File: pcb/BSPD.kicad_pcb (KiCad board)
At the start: 4 copper layers, 45 x 92.5 mm, 69 parts, among them J1 Test header, J2 Conn_02x06_Counter_Clockwise, Q1 AO3400A, U1 LM339, U2 LM339, U3 74HC32, U4 74HC02, U5 AMS1117-5.0, U6 AMS1117-5.0

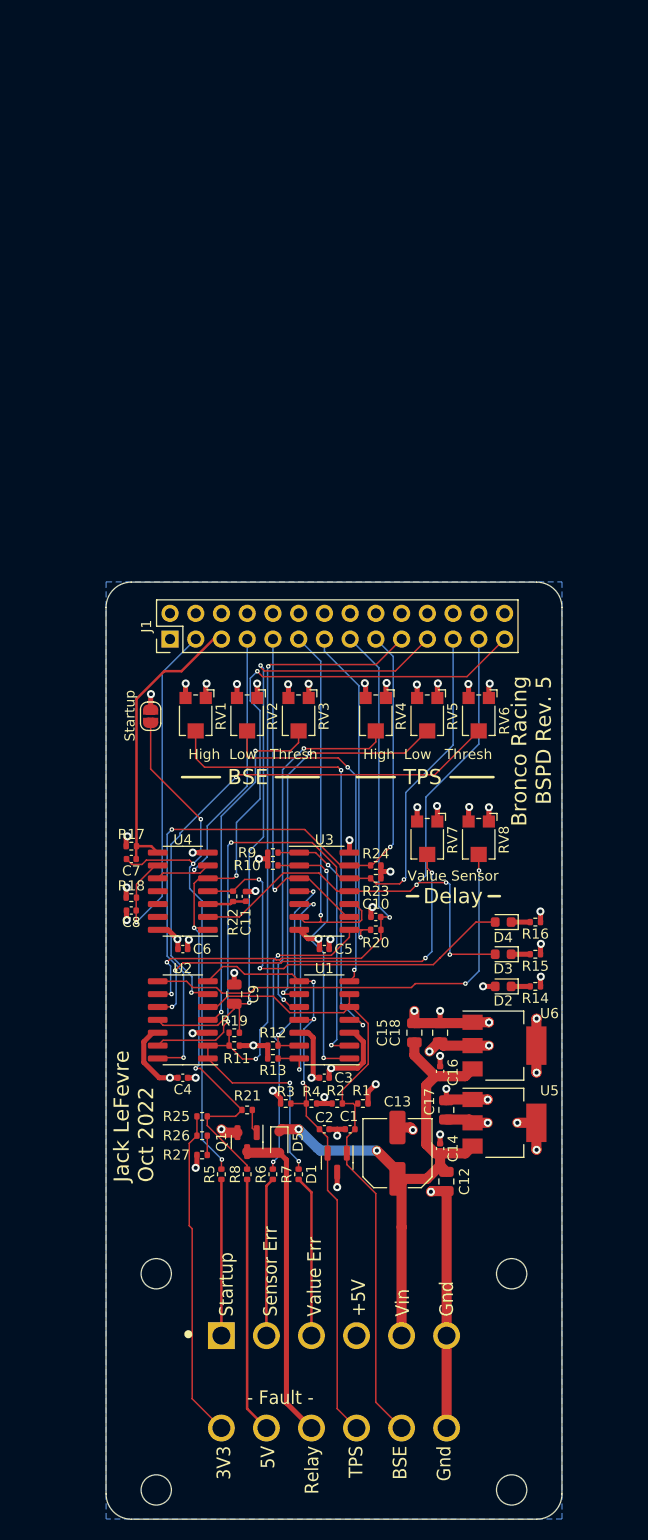
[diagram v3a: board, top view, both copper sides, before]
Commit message: Switch to M12 Connector, fix comparator issue from rev 5
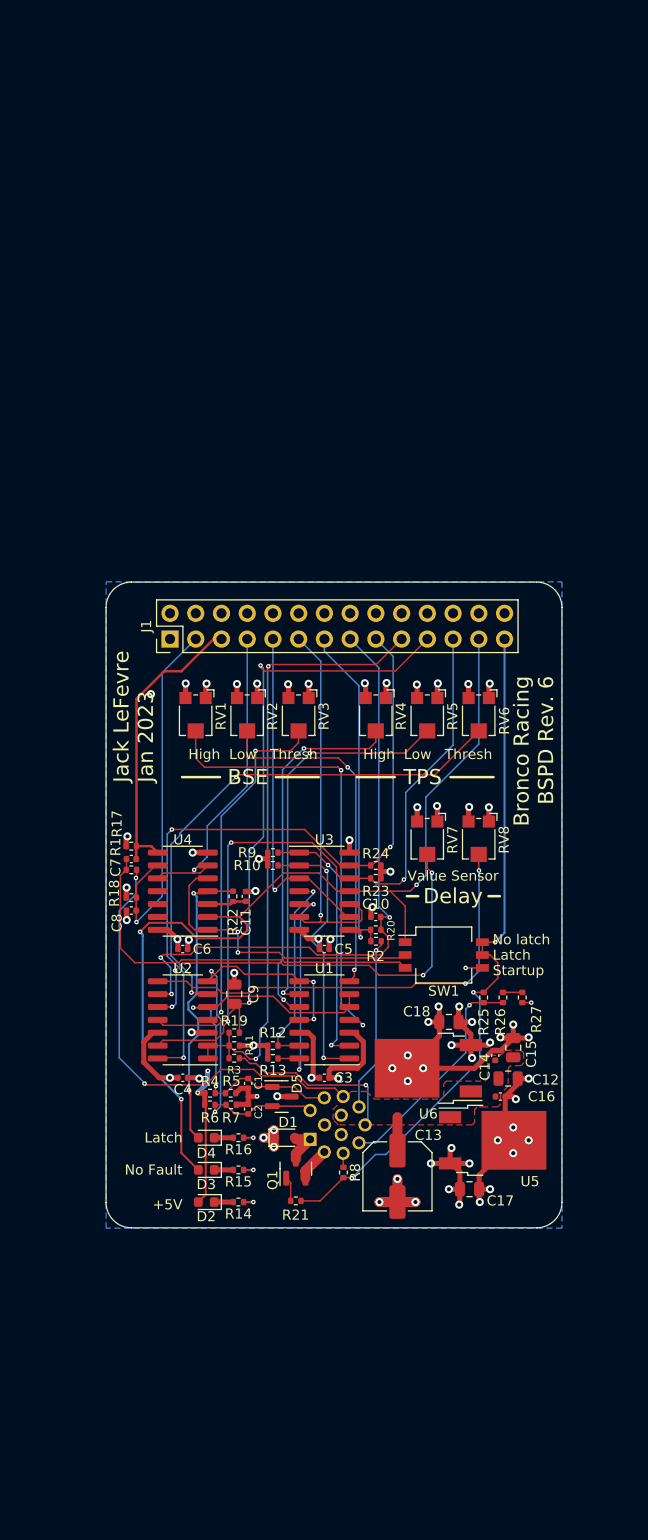
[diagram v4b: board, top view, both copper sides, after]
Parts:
- removed JP1: SolderJumper_2_Open, Jumper:SolderJumper-2_P1.3mm_Open_RoundedPad1.0x1.5mm
- added SW1: SW_DIP_x03, Button_Switch_SMD:SW_DIP_SPSTx03_Slide_KingTek_DSHP03TS_W7.62mm_P1.27mm, F.Cu at (145.8, 119.3)
- J2: value Conn_02x06_Counter_Clockwise -> T4142012121-000; footprint libraries:TE_DT15-12PA -> M12_TE_T4142012121-000:T4140012121000; moved to B.Cu
- R1, R2, R3: value 100k -> 1k
- R5, R6, R7: value 1k -> 100k
- U5, U6: value AMS1117-5.0 -> L7805; footprint Package_TO_SOT_SMD:SOT-223-3_TabPin2 -> Package_TO_SOT_SMD:TO-252-2
- moved D3 36.2 mm to (122.4, 140.5)
- moved D2 36.2 mm to (122.4, 143.7)
- moved D4 36.2 mm to (122.4, 137.3)
- moved R15 36.2 mm to (125.6, 140.5)
- moved R14 36.2 mm to (125.6, 143.7)
- moved R16 36.2 mm to (125.6, 137.3)
- moved R27 35.2 mm to (153.6, 123.5), turned to -90 degrees
- moved R26 32.7 mm to (151.7, 123.5), turned to 90 degrees
- moved R1 32.5 mm to (115.0, 110.9)
- moved R25 30.2 mm to (149.8, 123.5), turned to 90 degrees
- moved J2 24.1 mm to (132.6, 137.5)
- moved R2 16.5 mm to (139.2, 118.0)
- moved C12 11.8 mm to (152.2, 131.5), turned to 0 degrees
- moved C1 11.0 mm to (126.5, 132.0), turned to -90 degrees
- moved C14 10.7 mm to (150.9, 129.2)
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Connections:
- C3 pad 1: +5V -> Vin
- C4 pad 1: +5V -> Vin
- J2 pad 1: Net-(J2-Pad1) -> FAULT_12V
- J2 pad 10: FAULT_12V -> GND
- J2 pad 11: Net-(J2-Pad11) -> Vin
- J2 pad 12: FAULT_3V3 -> +5VE
- J2 pad 2: Net-(J2-Pad2) -> TPS_in
- J2 pad 3: Net-(J2-Pad3) -> BSE_in
- J2 pad 4: +5VE -> Net-(J2-Pad4)
- J2 pad 5: Vin -> Net-(J2-Pad5)
- J2 pad 6: GND -> Net-(J2-Pad6)
- J2 pad 7: GND -> FAULT_3V3
- J2 pad 8: BSE_in -> Net-(J2-Pad8)
- J2 pad 9: TPS_in -> GND
- R1 pad 1: +5V -> Net-(J2-Pad4)
- R1 pad 2: BSE_in -> Startup
- R2 pad 1: BSE_in -> Net-(J2-Pad5)
- R2 pad 2: GND -> Sensor Error
- R3 pad 1: +5V -> Net-(J2-Pad6)
- R3 pad 2: TPS_in -> Value Error
- R4 pad 1: TPS_in -> +5V
- R4 pad 2: GND -> BSE_in
- R5 pad 1: Net-(J2-Pad1) -> BSE_in
- R5 pad 2: Startup -> GND
- R6 pad 1: Net-(J2-Pad2) -> +5V
- R6 pad 2: Sensor Error -> TPS_in
- R7 pad 1: Net-(J2-Pad3) -> TPS_in
- R7 pad 2: Value Error -> GND
- R8 pad 1: Net-(J2-Pad11) -> Net-(J2-Pad8)
- U1 pad 3: +5V -> Vin
- U2 pad 3: +5V -> Vin
- U4 pad 1: FAULT_5V -> FAULT_LATCHING
- U4 pad 5: FAULT_5V -> FAULT_LATCHING
- U5 pad 1: GND -> Vin
- U5 pad 2: +5VE -> GND
- U5 pad 3: Vin -> +5VE
- U6 pad 1: GND -> Vin
- U6 pad 2: +5V -> GND
- U6 pad 3: Vin -> +5V
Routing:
- net Net-(J2-Pad4): track 0.00 -> 44.2 mm, vias 0 -> 2
- net Vin: track 57.2 -> 22.3 mm, vias 2 -> 6
- net Post-Delay: track 65.1 -> 95.2 mm
- net FAULT_LATCHING: track 0.00 -> 30.0 mm, vias 0 -> 2
- net Sensor Error: track 64.1 -> 35.0 mm, vias 3 -> 1
- net FAULT_12V: track 31.7 -> 4.12 mm
- net Net-(J2-Pad11): track 25.3 -> 0.00 mm
- net BSE_in: track 62.9 -> 39.6 mm, vias 0 -> 2
- net FAULT_5V: track 88.2 -> 69.6 mm, vias 4 -> 3
- net TPS_in: track 61.4 -> 43.4 mm, vias 3 -> 4
- net Net-(J2-Pad6): track 0.00 -> 17.7 mm, vias 0 -> 1
- net Net-(J2-Pad5): track 0.00 -> 17.3 mm, vias 0 -> 1
- net Startup: track 55.0 -> 38.2 mm, vias 3 -> 0
- net Value Error: track 79.3 -> 62.6 mm, vias 4 -> 2
- net Net-(J2-Pad3): track 15.9 -> 0.00 mm
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- added copper zone on F.Cu, net Vin
- added copper zone on In2.Cu, net Vin
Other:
- board size 45 x 92.5 mm -> 45 x 63.7 mm
- board text added: "+5V"
- board text added: "Bronco Racing BSPD Rev. 6"
- board text added: "Jack LeFevre Jan 2023"
- board text added: "Latch"
- board text added: "No Fault"
- board text added: "No latch"
- board text removed: "- Fault -"
- board text removed: "3V3 5V Relay TPS BSE Gnd"
- board text removed: "Bronco Racing BSPD Rev. 5"
- board text removed: "Jack LeFevre Oct 2022"
- board text removed: "Startup Sensor Err Value Err +5V Vin Gnd"

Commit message: Update to KiCad 7, bump project revision/date
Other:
- board text added: "Bronco Racing BSPD Rev. 6.1"
- board text added: "Jack LeFevre Aug 2023"
- board text removed: "Bronco Racing BSPD Rev. 6"
- board text removed: "Jack LeFevre Jan 2023"

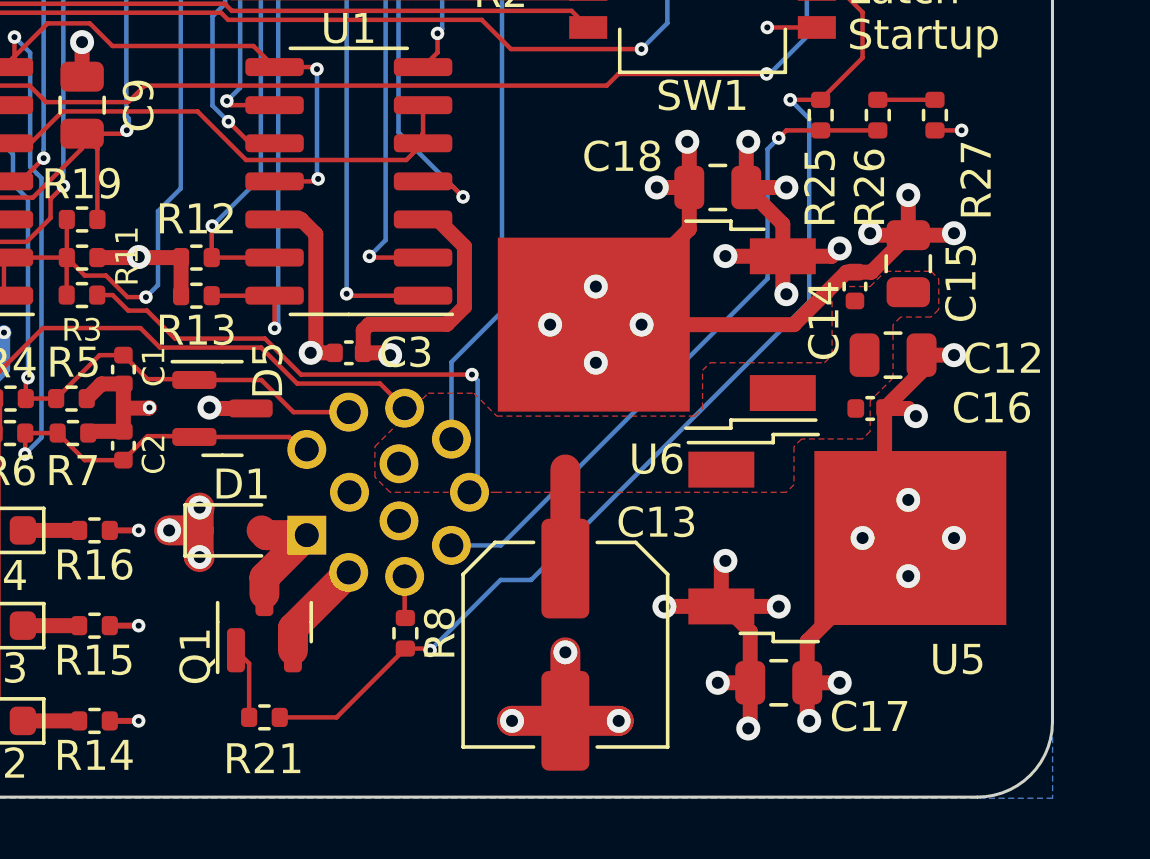
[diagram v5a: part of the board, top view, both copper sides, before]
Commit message: Fixed violations after kicad version bump
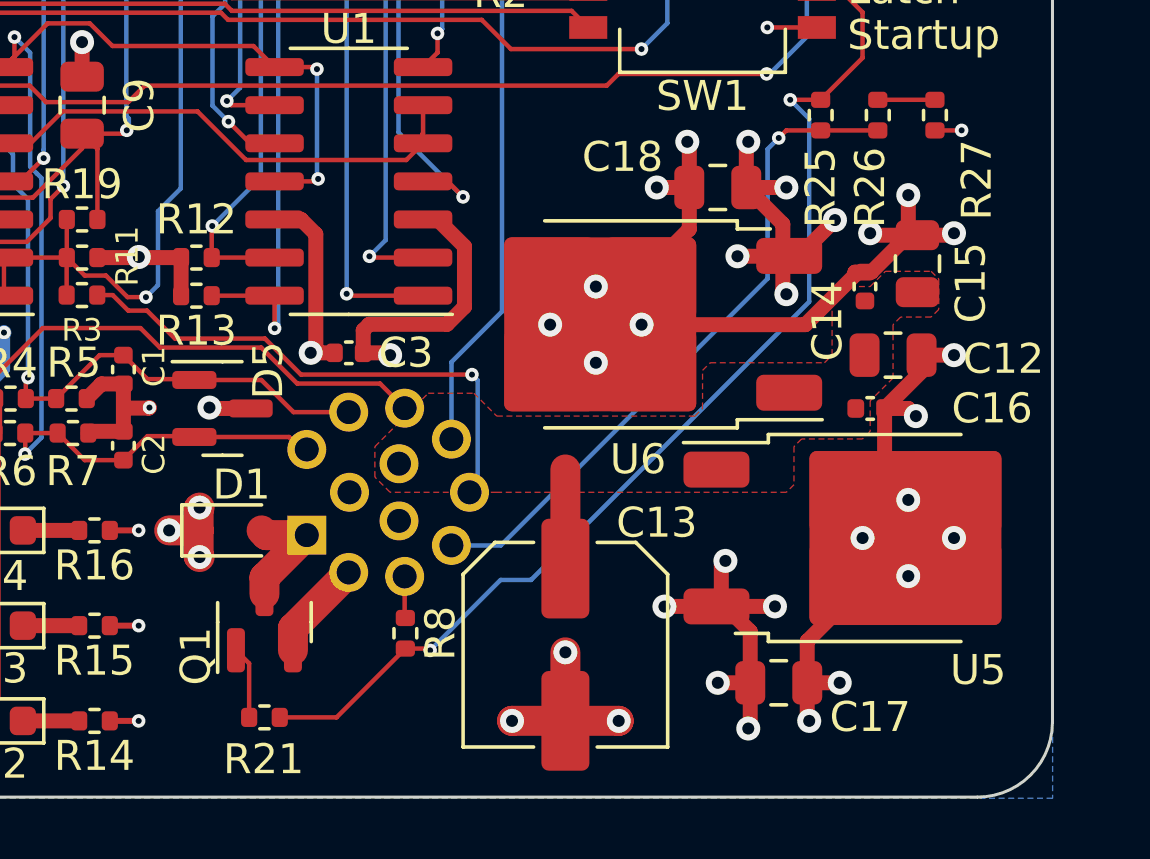
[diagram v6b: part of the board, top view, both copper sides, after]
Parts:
- SW1: value SW_DIP_x03 -> DSHP03TSGET
- moved U5 0.68 mm to (151.3, 137.6)
- moved U6 0.63 mm to (143.7, 130.5)
- moved C14 0.33 mm to (151.2, 129.2)
- moved C15 0.31 mm to (153.0, 128.5)

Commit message: fix missing footprint
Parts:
- G***: value LOGO -> electron; footprint LOGO -> electron:electron
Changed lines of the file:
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@@
         (effects (font (size 1 1) (thickness 0.15)))
+    )
+    (fp_text user "${REFERENCE}" (at 1.85 0 90) (layer "F.Fab")
+        (effects (font (size 0.8 0.8) (thickness 0.12)))
     )
     (fp_text user "on" (at -0.055 -2.1875) (layer "F.Fab")
-        (effects (font (size 0.8 0.8) (thickness 0.12)))
-    )
-    (fp_text user "${REFERENCE}" (at 1.85 0 90) (layer "F.Fab")
         (effects (font (size 0.8 0.8) (thickness 0.12)))
     )
@@
     )
   )
-  (footprint "LOGO" (layer "B.Cu")
+  (footprint "electron:electron" (layer "B.Cu")
     (at 134.406 119.056 -90)
     (attr board_only exclude_from_pos_files exclude_from_bom)
-    (fp_text reference "G***" (at 0 0) (layer "B.SilkS") hide
+    (fp_text reference "G***" (at 0 0 180) (layer "B.SilkS") hide
         (effects (font (size 1.524 1.524) (thickness 0.3)) (justify mirror))
     )
-    (fp_text value "LOGO" (at 0.75 0 -270) (layer "B.SilkS") hide
+    (fp_text value "electron" (at 0.75 0 90) (layer "B.SilkS") hide
         (effects (font (size 1.524 1.524) (thickness 0.3)) (justify mirror))
     )
